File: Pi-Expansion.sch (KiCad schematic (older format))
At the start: 16 parts, among them J1 RPi_GPIO, J2 MMCX_H, P1 BATT, U1 A2200-A, U2 SPX2920U-5.0

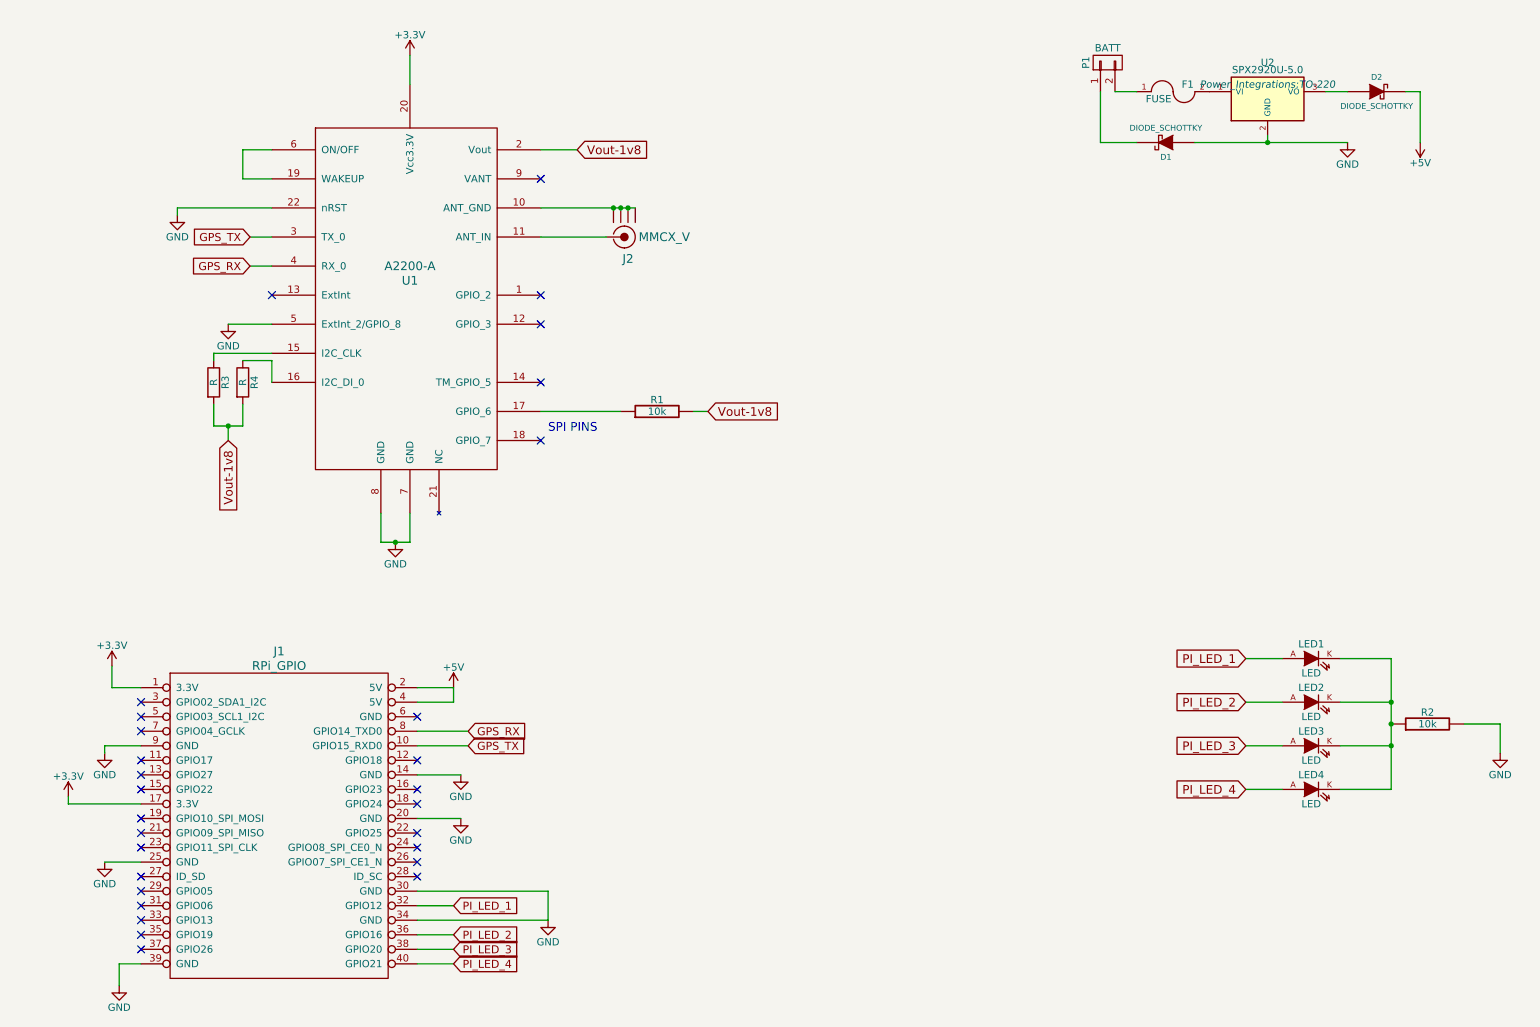
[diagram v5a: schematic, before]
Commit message: Made minor tweaks to schematic layout, updated footprints and  tweaked pcb layout
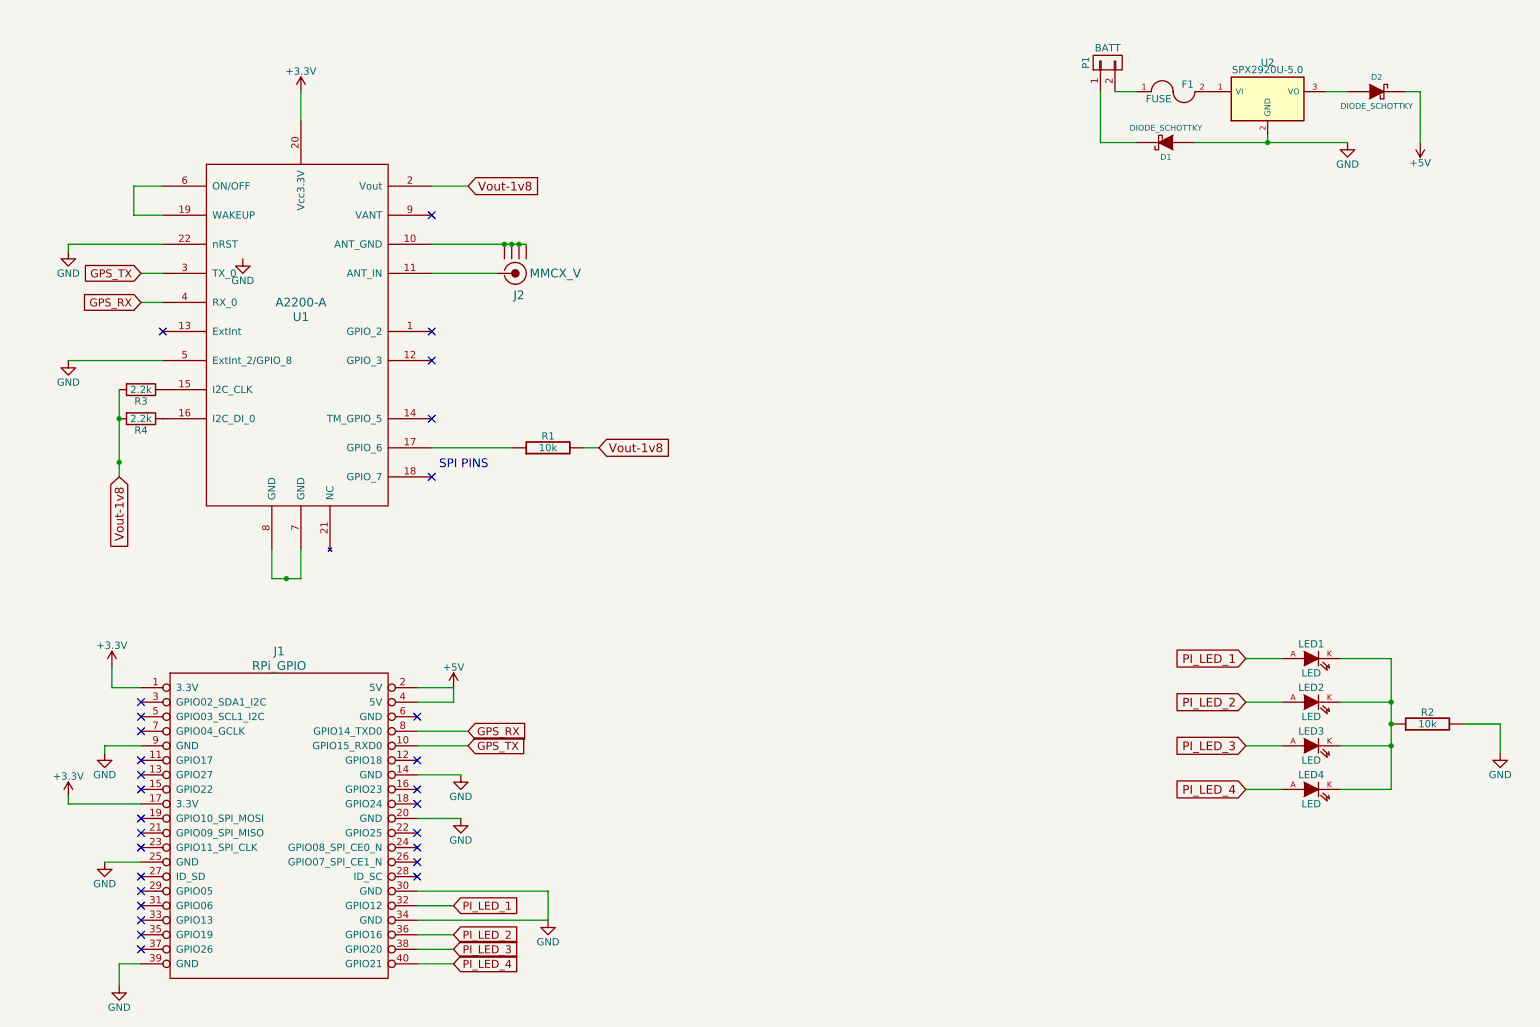
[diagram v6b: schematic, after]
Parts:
- D1, D2: footprint (none) -> Diodes_SMD:DO-214AB_Handsoldering
- R3, R4: value R -> 2.2k; footprint (none) -> Resistors_SMD:R_1206_HandSoldering
- U2: footprint Power_Integrations:TO-220 -> Converters_DCDC_ACDC:DCDC-Conv_Recom_R-78HBxx-0.5
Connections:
- net GND: no longer U1.7 (GND), U1.8 (GND)
- new net: U1.7 (GND), U1.8 (GND)
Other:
- moved on the sheet: J2, R1, R3, R4, U1

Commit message: First draft pcb layout, most tracks in place, footprints in near final positions
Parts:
- D1, D2: footprint Diodes_SMD:DO-214AB_Handsoldering -> Diodes_SMD:SOD-323
- R3, R4: footprint Resistors_SMD:R_1206_HandSoldering -> FT:1206
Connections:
- net +3V3: now also U1.22 (nRST)
- net GND: now also J1.6 (GND); no longer U1.22 (nRST)
- no-connect marks 29 -> 28
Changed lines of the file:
@@
 NoConn ~ 1650 2750
 NoConn ~ 3500 1950
-NoConn ~ 3400 5400
 NoConn ~ 1500 5900
 NoConn ~ 1500 5800
@@
 F 0 "D2" H 10000 1200 40  0000 C CNN
 F 1 "DIODE_SCHOTTKY" H 10000 1000 40  0000 C CNN
-F 2 "Diodes_SMD:DO-214AB_Handsoldering" H 10000 1100 60  0001 C CNN
+F 2 "Diodes_SMD:SOD-323" H 10000 1100 60  0001 C CNN
 F 3 "" H 10000 1100 60  0000 C CNN
 	1    10000 1100
@@
 F 0 "R4" V 1580 3350 50  0000 C CNN
 F 1 "2.2k" V 1500 3350 50  0000 C CNN
-F 2 "Resistors_SMD:R_1206_HandSoldering" V 1430 3350 50  0001 C CNN
+F 2 "FT:1206" V 1430 3350 50  0001 C CNN
 F 3 "" H 1500 3350 50  0000 C CNN
 	1    1500 3350
@@
 F 0 "R3" V 1580 3150 50  0000 C CNN
 F 1 "2.2k" V 1500 3150 50  0000 C CNN
-F 2 "Resistors_SMD:R_1206_HandSoldering" V 1430 3150 50  0001 C CNN
+F 2 "FT:1206" V 1430 3150 50  0001 C CNN
 F 3 "" H 1500 3150 50  0000 C CNN
 	1    1500 3150
@@
 Wire Wire Line
 	4550 3550 4650 3550
-$Comp
-L GND #PWR016
-U 1 1 573A4B6B
-P 1000 2200
-F 0 "#PWR016" H 1000 1950 50  0001 C CNN
-F 1 "GND" H 1000 2050 50  0000 C CNN
-F 2 "" H 1000 2200 50  0000 C CNN
-F 3 "" H 1000 2200 50  0000 C CNN
-	1    1000 2200
-	1    0    0    -1
-$EndComp
 Wire Wire Line
 	1650 2150 1000 2150
-Wire Wire Line
-	1000 2150 1000 2200
 NoConn ~ 3400 5700
 NoConn ~ 3400 5900
@@
 F 0 "D1" H 8550 1550 40  0000 C CNN
 F 1 "DIODE_SCHOTTKY" H 8550 1350 40  0000 C CNN
-F 2 "Diodes_SMD:DO-214AB_Handsoldering" H 8550 1450 60  0001 C CNN
+F 2 "Diodes_SMD:SOD-323" H 8550 1450 60  0001 C CNN
 F 3 "" H 8550 1450 60  0000 C CNN
 	1    8550 1450
@@
 	8100 1450 8350 1450
 Connection ~ 1350 3350
+Wire Wire Line
+	3700 5800 3700 5400
+Wire Wire Line
+	3700 5400 3400 5400
+$Comp
+L +3.3V #PWR?
+U 1 1 573DF9C6
+P 1000 2150
+F 0 "#PWR?" H 1000 2000 50  0001 C CNN
+F 1 "+3.3V" H 1000 2290 50  0000 C CNN
+F 2 "" H 1000 2150 50  0000 C CNN
+F 3 "" H 1000 2150 50  0000 C CNN
+	1    1000 2150
+	1    0    0    -1
+$EndComp
 $EndSCHEMATC

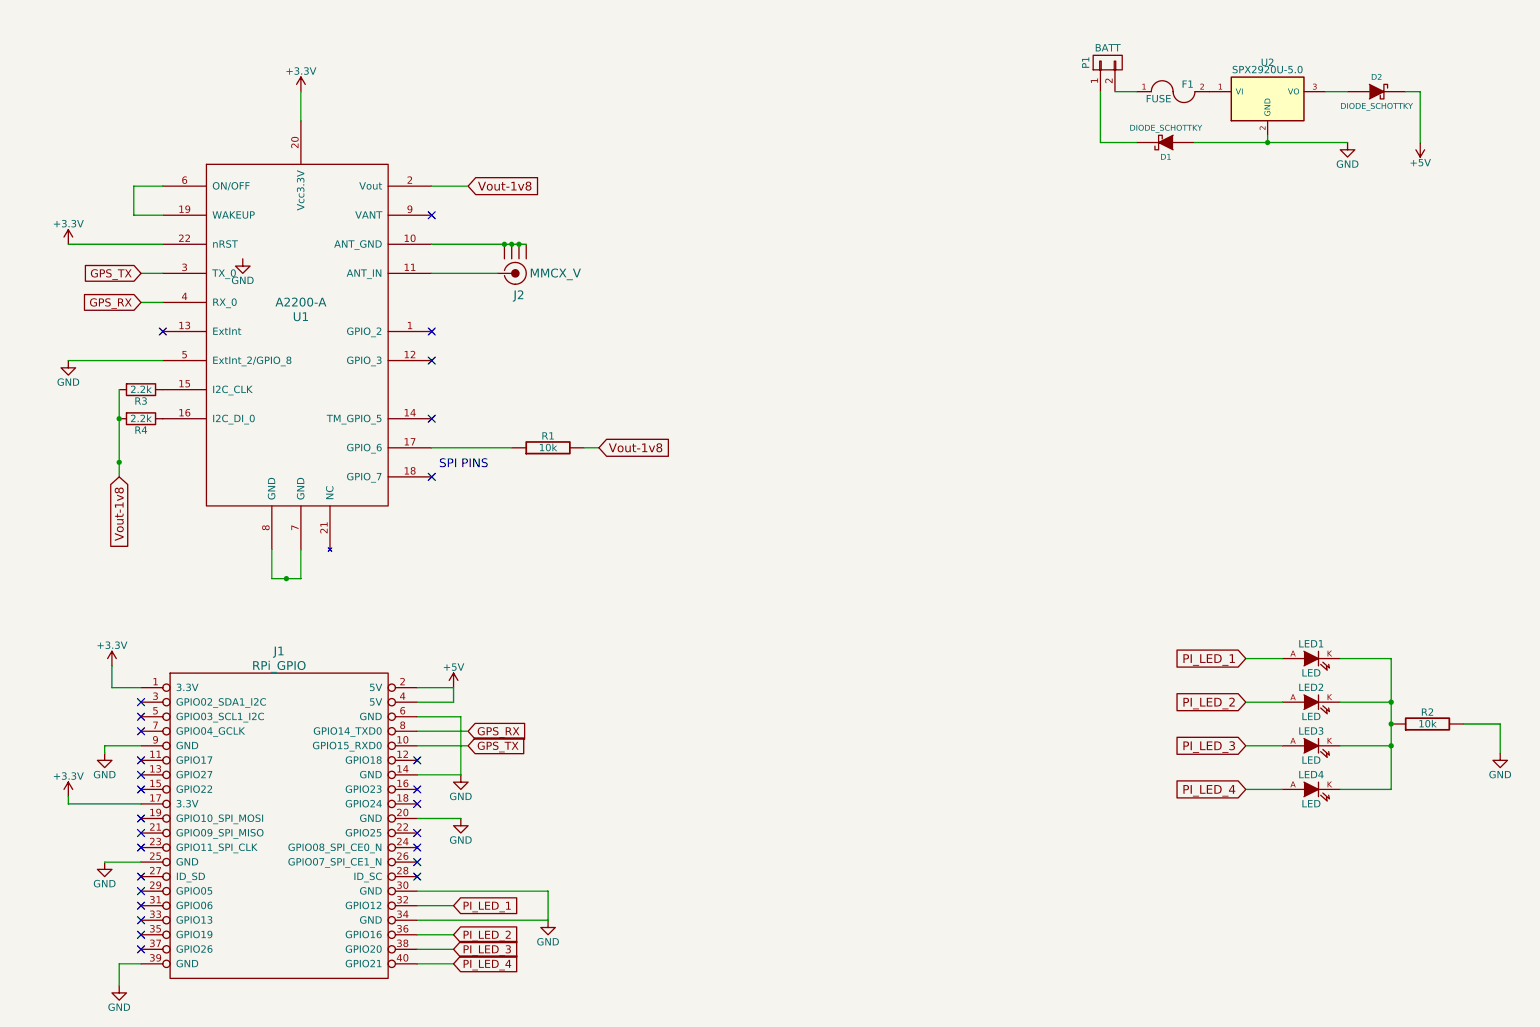
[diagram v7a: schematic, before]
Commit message: Final Layout, Traces and footprints in place, added GPS_TX sensing circuit 3.3v powerled.
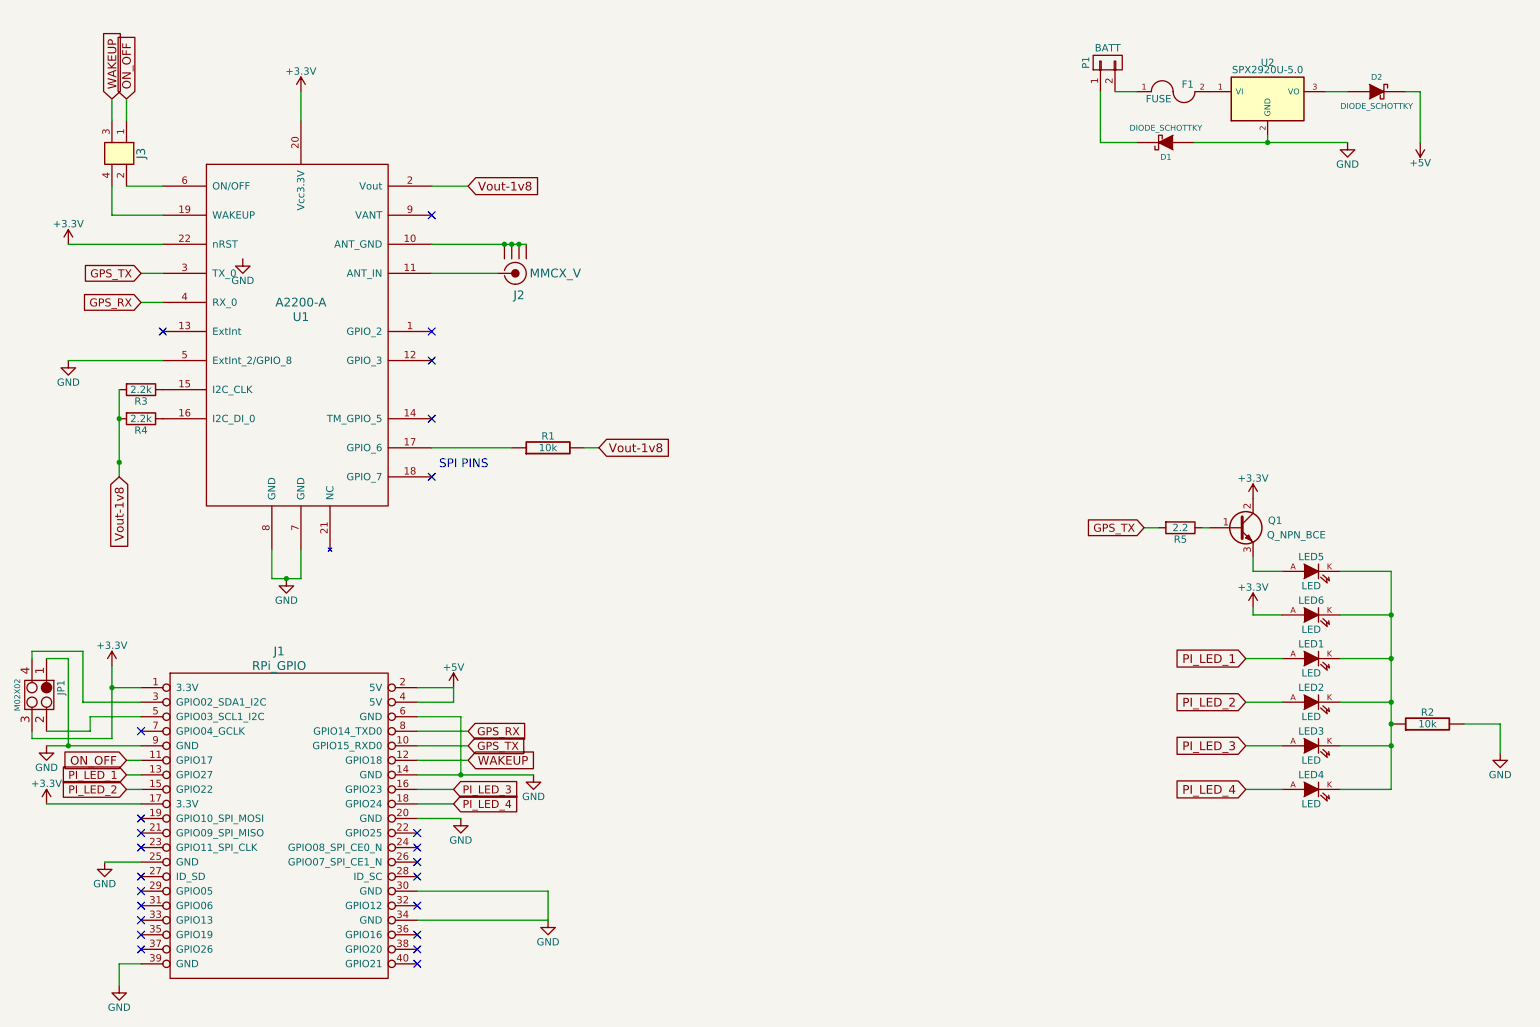
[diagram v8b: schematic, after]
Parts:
- added J3: PINHEADER_2X2_SMD, Pinhead_2x2_SMD, symbol PINHEADER_2X2_SMD
- added JP1: M02X02, Sockets_MOLEX_KK-System:Socket_MOLEX-KK-RM2-54mm_Lock_4pin_straight, symbol M02X02
- added LED5, LED6: LED, FT:LED-1206, symbol LED-RESCUE-Pi-Expansion
- added Q1: Q_NPN_BCE, TO_SOT_Packages_SMD:SOT-23, symbol Q_NPN_BCE
- added R5: 2.2, Resistors_SMD:R_1206, symbol R
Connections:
- net +3V3: now also JP1.3, LED6.A, Q1.2 (C)
- net GND: now also U1.7 (GND), U1.8 (GND), JP1.1
- net GPS_TX: now also R5.2
- net PI_LED_1: now also J1.13 (GPIO27); no longer J1.32 (GPIO12)
- net PI_LED_2: now also J1.15 (GPIO22); no longer J1.36 (GPIO16)
- net PI_LED_3: now also J1.16 (GPIO23); no longer J1.38 (GPIO20)
- net PI_LED_4: now also J1.18 (GPIO24); no longer J1.40 (GPIO21)
- net at U1.19 (WAKEUP): now also J3.4; no longer U1.6 (ON/OFF)
- net ON_OFF: now reaches J1.11 (GPIO17)
- net ON_OFF: now also J3.1
- net WAKEUP: now reaches J1.12 (GPIO18)
- net WAKEUP: now also J3.3
- net at J1.3 (GPIO02_SDA1_I2C): now also JP1.4
- net at J1.5 (GPIO03_SCL1_I2C): now also JP1.2
- net at LED1.K, LED2.K, LED3.K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: now also LED5.K, LED6.K
- new net: J3.2, U1.6 (ON/OFF)
- new net: LED5.A, Q1.3 (E)
- new net: Q1.1 (B), R5.1
- no-connect marks 28 -> 24
